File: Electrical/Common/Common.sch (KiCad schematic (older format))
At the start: 68 parts, among them J201 01x02, J202 01x04, J203 01x03, J204 01x04, J205 01x03, J206 USB_OTG, J207 01x04, J208 01x02, J209 01x04, J210 01x02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

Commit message: Completed Dual Stepper Layout. TODO: Via stitching.
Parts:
- removed J215: JST_3, Connectors_JST:JST_XH_B03B-XH-A_03x2.50mm_Straight, symbol Conn_01x03
- added J217: 2PostTerm, footprints:TerminalBlock_Custom_1x02.54mm, symbol Screw_Terminal_01x02
- added J218, J219: 01x02, Pin_Headers:Pin_Header_Straight_1x02_Pitch2.54mm, symbol Conn_01x02
- added R205, R206: 12K, Resistors_SMD:R_0603_HandSoldering, symbol R
- added RN208, RN209, RN210, RN211: 1K2, footprints:R_Array_1206x04, symbol R_Pack04
- J206: footprint Connectors_USB:USB_Micro-B_Molex-105017-0001 -> footprints:USB_Micro-B_Molex-105017-0001_CircularHoles
- renumbered J216 to J215, J217 to J216
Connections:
- net labels added: GPIO_52, gpio1_12, usb1_5V
- net labels removed: +BATT, GPIO_44, batt_temp, gpio1_20
- wire segments 263 -> 286
- no-connect marks 2 -> 4
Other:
- moved on the sheet: J213, J214, J215, J216

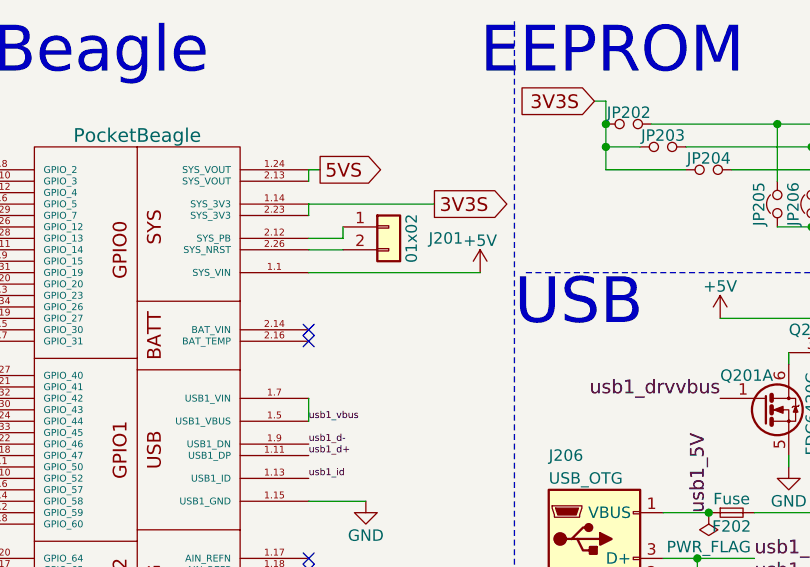
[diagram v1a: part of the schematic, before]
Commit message: Added a diode to the stepper fault/3v3 supply to ensure fault remains low when RESET/PMIC_OUT_PGOOD is low.
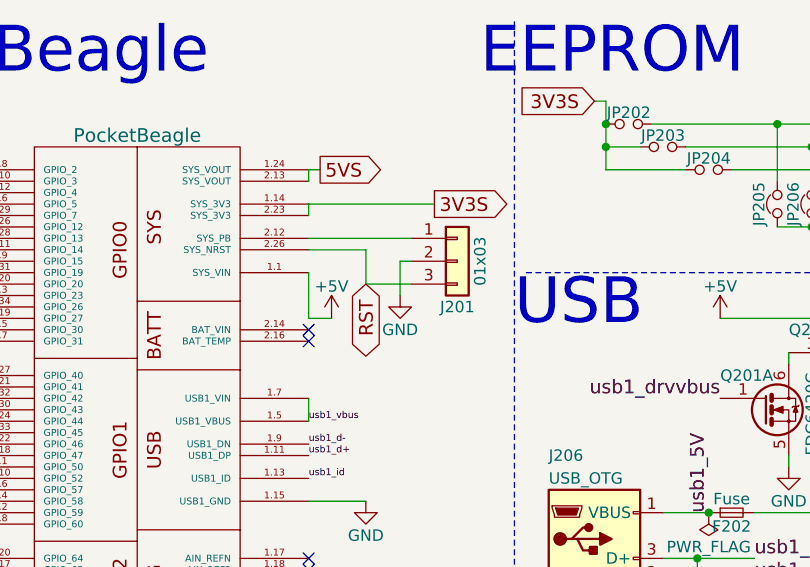
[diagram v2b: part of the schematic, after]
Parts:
- removed J201: 01x02, Pin_Headers:Pin_Header_Straight_1x02_Pitch2.54mm, symbol Conn_01x02
- added J201: 01x03, Pin_Headers:Pin_Header_Straight_1x03_Pitch2.54mm, symbol Conn_01x03
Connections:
- net labels added: RST
- wire segments 286 -> 290

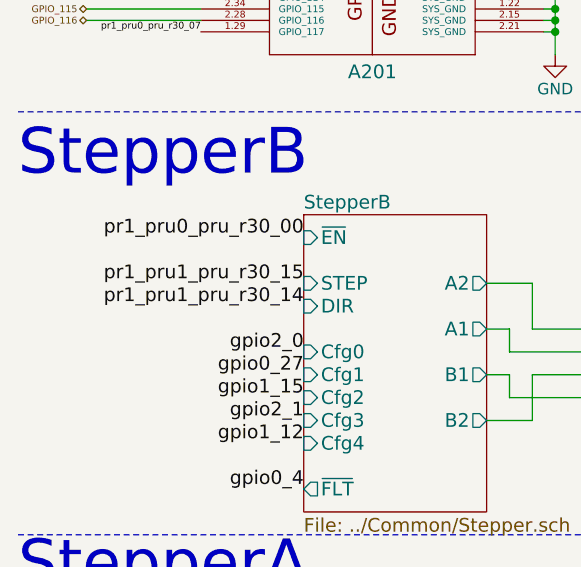
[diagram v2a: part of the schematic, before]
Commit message: Switched two pins for easier routing on quad board.
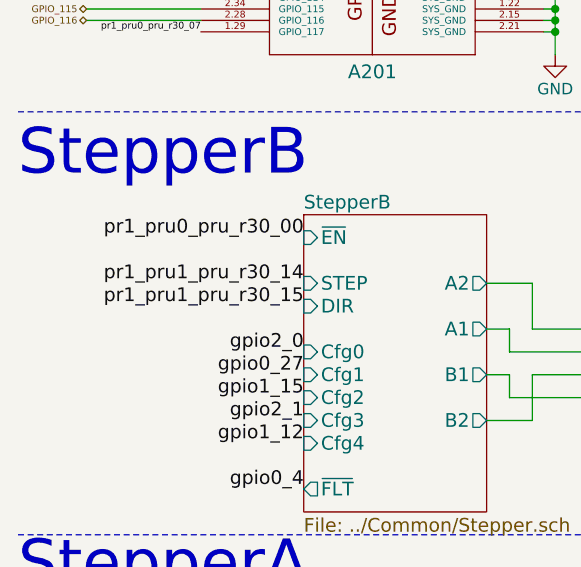
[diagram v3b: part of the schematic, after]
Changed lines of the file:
@@
 LIBS:allegro
 LIBS:mechanical
-LIBS:Dual-cache
+LIBS:Quad-cache
 EELAYER 25 0
 EELAYER END
 $Descr A4 11693 8268
 encoding utf-8
-Sheet 2 4
+Sheet 2 6
 Title ""
 Date ""
@@
 Adjustable Power Supply
 $Comp
-L GND #PWR211
+L GND #PWR04
 U 1 1 5A4ECB5E
 P 2850 3750
-F 0 "#PWR211" H 2850 3500 50  0001 C CNN
+F 0 "#PWR04" H 2850 3500 50  0001 C CNN
 F 1 "GND" H 2850 3600 50  0000 C CNN
 F 2 "" H 2850 3750 50  0001 C CNN
@@
 $EndComp
 $Comp
-L GND #PWR205
+L GND #PWR05
 U 1 1 5A5034AE
 P 8950 1900
-F 0 "#PWR205" H 8950 1650 50  0001 C CNN
+F 0 "#PWR05" H 8950 1650 50  0001 C CNN
 F 1 "GND" H 8950 1750 50  0000 C CNN
 F 2 "" H 8950 1900 50  0001 C CNN
@@
 $EndComp
 $Comp
-L GND #PWR210
+L GND #PWR06
 U 1 1 5A50411A
 P 8950 3550
-F 0 "#PWR210" H 8950 3300 50  0001 C CNN
+F 0 "#PWR06" H 8950 3300 50  0001 C CNN
 F 1 "GND" H 8950 3400 50  0000 C CNN
 F 2 "" H 8950 3550 50  0001 C CNN
@@
 $EndComp
 $Comp
-L PWR_FLAG #FLG202
+L PWR_FLAG #FLG07
 U 1 1 5A50A965
 P 7800 4350
-F 0 "#FLG202" H 7800 4425 50  0001 C CNN
+F 0 "#FLG07" H 7800 4425 50  0001 C CNN
 F 1 "PWR_FLAG" H 7800 4500 50  0000 C CNN
 F 2 "" H 7800 4350 50  0001 C CNN
@@
 Vin
 $Comp
-L GND #PWR219
+L GND #PWR08
 U 1 1 5A50A9F8
 P 7800 4900
-F 0 "#PWR219" H 7800 4650 50  0001 C CNN
+F 0 "#PWR08" H 7800 4650 50  0001 C CNN
 F 1 "GND" H 7800 4750 50  0000 C CNN
 F 2 "" H 7800 4900 50  0001 C CNN
@@
 Vadj
 $Comp
-L +5V #PWR212
+L +5V #PWR09
 U 1 1 5A50AB43
 P 8400 4250
-F 0 "#PWR212" H 8400 4100 50  0001 C CNN
+F 0 "#PWR09" H 8400 4100 50  0001 C CNN
 F 1 "+5V" H 8400 4390 50  0000 C CNN
 F 2 "" H 8400 4250 50  0001 C CNN
@@
 $EndComp
 $Comp
-L GND #PWR216
+L GND #PWR010
 U 1 1 5A50ABA3
 P 9150 4450
-F 0 "#PWR216" H 9150 4200 50  0001 C CNN
+F 0 "#PWR010" H 9150 4200 50  0001 C CNN
 F 1 "GND" H 9150 4300 50  0000 C CNN
 F 2 "" H 9150 4450 50  0001 C CNN
@@
 $EndComp
 $Comp
-L GND #PWR215
+L GND #PWR011
 U 1 1 5A50ABE1
 P 8400 4450
-F 0 "#PWR215" H 8400 4200 50  0001 C CNN
+F 0 "#PWR011" H 8400 4200 50  0001 C CNN
 F 1 "GND" H 8400 4300 50  0000 C CNN
 F 2 "" H 8400 4450 50  0001 C CNN
@@
 $EndComp
 $Comp
-L +5V #PWR223
+L +5V #PWR012
 U 1 1 5A50ACF1
 P 7250 5200
-F 0 "#PWR223" H 7250 5050 50  0001 C CNN
+F 0 "#PWR012" H 7250 5050 50  0001 C CNN
 F 1 "+5V" H 7250 5340 50  0000 C CNN
 F 2 "" H 7250 5200 50  0001 C CNN
@@
 $EndSheet
 $Comp
-L +5V #PWR203
+L +5V #PWR013
 U 1 1 5A55A7CC
 P 2900 1800
-F 0 "#PWR203" H 2900 1650 50  0001 C CNN
+F 0 "#PWR013" H 2900 1650 50  0001 C CNN
 F 1 "+5V" H 2900 1940 50  0000 C CNN
 F 2 "" H 2900 1800 50  0001 C CNN
@@
 Text Label 1750 4550 2    60   ~ 0
 pr1_pru0_pru_r30_00
+Text Label 1750 4850 2    60   ~ 0
+pr1_pru1_pru_r30_15
 Text Label 1750 4750 2    60   ~ 0
-pr1_pru1_pru_r30_15
-Text Label 1750 4850 2    60   ~ 0
 pr1_pru1_pru_r30_14
 Text Label 1750 5050 2    60   ~ 0
@@
 $EndComp
 $Comp
-L GND #PWR218
+L GND #PWR014
 U 1 1 5A57243C
 P 4950 4900
-F 0 "#PWR218" H 4950 4650 50  0001 C CNN
+F 0 "#PWR014" H 4950 4650 50  0001 C CNN
 F 1 "GND" H 4950 4750 50  0000 C CNN
 F 2 "" H 4950 4900 50  0001 C CNN
@@
 $EndComp
 $Comp
-L GND #PWR227
+L GND #PWR015
 U 1 1 5A57262A
 P 5400 5850
-F 0 "#PWR227" H 5400 5600 50  0001 C CNN
+F 0 "#PWR015" H 5400 5600 50  0001 C CNN
 F 1 "GND" H 5400 5700 50  0000 C CNN
 F 2 "" H 5400 5850 50  0001 C CNN
@@
 $EndComp
 $Comp
-L GND #PWR213
+L GND #PWR016
 U 1 1 5A576111
 P 6300 4400
-F 0 "#PWR213" H 6300 4150 50  0001 C CNN
+F 0 "#PWR016" H 6300 4150 50  0001 C CNN
 F 1 "GND" H 6300 4250 50  0000 C CNN
 F 2 "" H 6300 4400 50  0001 C CNN
@@
 AIN_5V_3
 $Comp
-L GND #PWR231
+L GND #PWR017
 U 1 1 5A57FE72
 P 4800 7600
-F 0 "#PWR231" H 4800 7350 50  0001 C CNN
+F 0 "#PWR017" H 4800 7350 50  0001 C CNN
 F 1 "GND" H 4800 7450 50  0000 C CNN
 F 2 "" H 4800 7600 50  0001 C CNN
@@
 $EndComp
 $Comp
-L GND #PWR222
+L GND #PWR018
 U 1 1 5A589958
 P 4350 5200
-F 0 "#PWR222" H 4350 4950 50  0001 C CNN
+F 0 "#PWR018" H 4350 4950 50  0001 C CNN
 F 1 "GND" H 4350 5050 50  0000 C CNN
 F 2 "" H 4350 5200 50  0001 C CNN
@@
 3V3S
 $Comp
-L GND #PWR201
+L GND #PWR019
 U 1 1 5A56CE51
 P 5800 1400
-F 0 "#PWR201" H 5800 1150 50  0001 C CNN
+F 0 "#PWR019" H 5800 1150 50  0001 C CNN
 F 1 "GND" H 5800 1250 50  0000 C CNN
 F 2 "" H 5800 1400 50  0001 C CNN
@@
 $EndComp
 $Comp
-L GND #PWR208
+L GND #PWR020
 U 1 1 5A581D55
 P 4200 3450
-F 0 "#PWR208" H 4200 3200 50  0001 C CNN
+F 0 "#PWR020" H 4200 3200 50  0001 C CNN
 F 1 "GND" H 4200 3300 50  0000 C CNN
 F 2 "" H 4200 3450 50  0001 C CNN
@@
 $EndComp
 $Comp
-L GND #PWR207
+L GND #PWR021
 U 1 1 5A582263
 P 3050 2600
-F 0 "#PWR207" H 3050 2350 50  0001 C CNN
+F 0 "#PWR021" H 3050 2350 50  0001 C CNN
 F 1 "GND" H 3050 2450 50  0000 C CNN
 F 2 "" H 3050 2600 50  0001 C CNN
@@
 usb1_d-
 $Comp
-L +5V #PWR204
+L +5V #PWR022
 U 1 1 5A583964
 P 4600 1800
-F 0 "#PWR204" H 4600 1650 50  0001 C CNN
+F 0 "#PWR022" H 4600 1650 50  0001 C CNN
 F 1 "+5V" H 4600 1940 50  0000 C CNN
 F 2 "" H 4600 1800 50  0001 C CNN
@@
 $EndComp
 $Comp
-L GND #PWR206
+L GND #PWR023
 U 1 1 5A586591
 P 4900 2450
-F 0 "#PWR206" H 4900 2200 50  0001 C CNN
+F 0 "#PWR023" H 4900 2200 50  0001 C CNN
 F 1 "GND" H 4900 2300 50  0000 C CNN
 F 2 "" H 4900 2450 50  0001 C CNN
@@
 	4500 3350 4400 3350
 $Comp
-L GND #PWR209
+L GND #PWR024
 U 1 1 5A5906F7
 P 5300 3450
-F 0 "#PWR209" H 5300 3200 50  0001 C CNN
+F 0 "#PWR024" H 5300 3200 50  0001 C CNN
 F 1 "GND" H 5300 3300 50  0000 C CNN
 F 2 "" H 5300 3450 50  0001 C CNN
@@
 $EndComp
 $Comp
-L GND #PWR214
+L GND #PWR025
 U 1 1 5A59F19E
 P 3200 4450
-F 0 "#PWR214" H 3200 4200 50  0001 C CNN
+F 0 "#PWR025" H 3200 4200 50  0001 C CNN
 F 1 "GND" H 3200 4300 50  0000 C CNN
 F 2 "" H 3200 4450 50  0001 C CNN
@@
 $EndComp
 $Comp
-L GND #PWR230
+L GND #PWR026
 U 1 1 5A59F7FF
 P 3700 6350
-F 0 "#PWR230" H 3700 6100 50  0001 C CNN
+F 0 "#PWR026" H 3700 6100 50  0001 C CNN
 F 1 "GND" H 3700 6200 50  0000 C CNN
 F 2 "" H 3700 6350 50  0001 C CNN
@@
 Connection ~ 7800 4800
 $Comp
-L PWR_FLAG #FLG203
+L PWR_FLAG #FLG027
 U 1 1 5A590642
 P 7950 4800
-F 0 "#FLG203" H 7950 4875 50  0001 C CNN
+F 0 "#FLG027" H 7950 4875 50  0001 C CNN
 F 1 "PWR_FLAG" H 7950 4950 50  0000 C CNN
 F 2 "" H 7950 4800 50  0001 C CNN
@@
 	7950 4800 7800 4800
 $Comp
-L PWR_FLAG #FLG204
+L PWR_FLAG #FLG028
 U 1 1 5A590F89
 P 7000 5100
-F 0 "#FLG204" H 7000 5175 50  0001 C CNN
+F 0 "#FLG028" H 7000 5175 50  0001 C CNN
 F 1 "PWR_FLAG" H 7000 5250 50  0000 C CNN
 F 2 "" H 7000 5100 50  0001 C CNN
@@
 Connection ~ 6700 5100
 $Comp
-L PWR_FLAG #FLG205
+L PWR_FLAG #FLG029
 U 1 1 5A5913B1
 P 6950 5200
-F 0 "#FLG205" H 6950 5275 50  0001 C CNN
+F 0 "#FLG029" H 6950 5275 50  0001 C CNN
 F 1 "PWR_FLAG" H 6950 5350 50  0000 C CNN
 F 2 "" H 6950 5200 50  0001 C CNN
@@
 Connection ~ 6950 5200
 $Comp
-L PWR_FLAG #FLG201
+L PWR_FLAG #FLG030
 U 1 1 5A592059
 P 4550 2650
-F 0 "#FLG201" H 4550 2725 50  0001 C CNN
+F 0 "#FLG030" H 4550 2725 50  0001 C CNN
 F 1 "PWR_FLAG" H 4550 2800 50  0000 C CNN
 F 2 "" H 4550 2650 50  0001 C CNN
@@
 $EndComp
 $Comp
-L GND #PWR229
+L GND #PWR031
 U 1 1 5A5A5D04
 P 8850 6300
-F 0 "#PWR229" H 8850 6050 50  0001 C CNN
+F 0 "#PWR031" H 8850 6050 50  0001 C CNN
 F 1 "GND" H 8850 6150 50  0000 C CNN
 F 2 "" H 8850 6300 50  0001 C CNN
@@
 $EndComp
 $Comp
-L GND #PWR220
+L GND #PWR032
 U 1 1 5A5BF7A7
 P 9150 5000
-F 0 "#PWR220" H 9150 4750 50  0001 C CNN
+F 0 "#PWR032" H 9150 4750 50  0001 C CNN
 F 1 "GND" H 9150 4850 50  0000 C CNN
 F 2 "" H 9150 5000 50  0001 C CNN
@@
 $EndComp
 $Comp
-L GND #PWR217
+L GND #PWR033
 U 1 1 5A5C0770
 P 10150 4450
-F 0 "#PWR217" H 10150 4200 50  0001 C CNN
+F 0 "#PWR033" H 10150 4200 50  0001 C CNN
 F 1 "GND" H 10150 4300 50  0000 C CNN
 F 2 "" H 10150 4450 50  0001 C CNN
@@
 $EndComp
 $Comp
-L GND #PWR221
+L GND #PWR034
 U 1 1 5A5E1379
 P 10150 5000
-F 0 "#PWR221" H 10150 4750 50  0001 C CNN
+F 0 "#PWR034" H 10150 4750 50  0001 C CNN
 F 1 "GND" H 10150 4850 50  0000 C CNN
 F 2 "" H 10150 5000 50  0001 C CNN
@@
 	9250 5500 9250 5700
 $Comp
-L GND #PWR224
+L GND #PWR035
 U 1 1 5A5EB0DE
 P 9250 5700
-F 0 "#PWR224" H 9250 5450 50  0001 C CNN
+F 0 "#PWR035" H 9250 5450 50  0001 C CNN
 F 1 "GND" H 9250 5550 50  0000 C CNN
 F 2 "" H 9250 5700 50  0001 C CNN
@@
 	10750 5500 10750 5700
 $Comp
-L GND #PWR226
+L GND #PWR036
 U 1 1 5A5EBF7E
 P 10750 5700
-F 0 "#PWR226" H 10750 5450 50  0001 C CNN
+F 0 "#PWR036" H 10750 5450 50  0001 C CNN
 F 1 "GND" H 10750 5550 50  0000 C CNN
 F 2 "" H 10750 5700 50  0001 C CNN
@@
 	10150 5500 10150 6300
 $Comp
-L GND #PWR225
+L GND #PWR037
 U 1 1 5A5EF63A
 P 9750 5700
-F 0 "#PWR225" H 9750 5450 50  0001 C CNN
+F 0 "#PWR037" H 9750 5450 50  0001 C CNN
 F 1 "GND" H 9750 5550 50  0000 C CNN
 F 2 "" H 9750 5700 50  0001 C CNN
@@
 	10750 5950 10650 5950
 $Comp
-L GND #PWR228
+L GND #PWR038
 U 1 1 5A5F1ED1
 P 10650 6150
-F 0 "#PWR228" H 10650 5900 50  0001 C CNN
+F 0 "#PWR038" H 10650 5900 50  0001 C CNN
 F 1 "GND" H 10650 6000 50  0000 C CNN
 F 2 "" H 10650 6150 50  0001 C CNN
@@
 	3050 1650 3250 1650
 $Comp
-L GND #PWR202
+L GND #PWR039
 U 1 1 5A62C26E
 P 3200 1700
-F 0 "#PWR202" H 3200 1450 50  0001 C CNN
+F 0 "#PWR039" H 3200 1450 50  0001 C CNN
 F 1 "GND" H 3200 1550 50  0000 C CNN
 F 2 "" H 3200 1700 50  0001 C CNN

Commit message: fixed unconnected pad 6 on RN201
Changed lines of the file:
@@
 LIBS:allegro
 LIBS:mechanical
-LIBS:Quad-cache
+LIBS:Dual-cache
 EELAYER 25 0
 EELAYER END
 $Descr A4 11693 8268
 encoding utf-8
-Sheet 2 6
+Sheet 2 4
 Title ""
 Date ""
@@
 Adjustable Power Supply
 $Comp
-L GND #PWR04
+L GND #PWR06
 U 1 1 5A4ECB5E
 P 2850 3750
-F 0 "#PWR04" H 2850 3500 50  0001 C CNN
+F 0 "#PWR06" H 2850 3500 50  0001 C CNN
 F 1 "GND" H 2850 3600 50  0000 C CNN
 F 2 "" H 2850 3750 50  0001 C CNN
@@
 $EndComp
 $Comp
-L GND #PWR05
+L GND #PWR07
 U 1 1 5A5034AE
 P 8950 1900
-F 0 "#PWR05" H 8950 1650 50  0001 C CNN
+F 0 "#PWR07" H 8950 1650 50  0001 C CNN
 F 1 "GND" H 8950 1750 50  0000 C CNN
 F 2 "" H 8950 1900 50  0001 C CNN
@@
 $EndComp
 $Comp
-L GND #PWR06
+L GND #PWR08
 U 1 1 5A50411A
 P 8950 3550
-F 0 "#PWR06" H 8950 3300 50  0001 C CNN
+F 0 "#PWR08" H 8950 3300 50  0001 C CNN
 F 1 "GND" H 8950 3400 50  0000 C CNN
 F 2 "" H 8950 3550 50  0001 C CNN
@@
 $EndComp
 $Comp
-L PWR_FLAG #FLG07
+L PWR_FLAG #FLG09
 U 1 1 5A50A965
 P 7800 4350
-F 0 "#FLG07" H 7800 4425 50  0001 C CNN
+F 0 "#FLG09" H 7800 4425 50  0001 C CNN
 F 1 "PWR_FLAG" H 7800 4500 50  0000 C CNN
 F 2 "" H 7800 4350 50  0001 C CNN
@@
 Vin
 $Comp
-L GND #PWR08
+L GND #PWR010
 U 1 1 5A50A9F8
 P 7800 4900
-F 0 "#PWR08" H 7800 4650 50  0001 C CNN
+F 0 "#PWR010" H 7800 4650 50  0001 C CNN
 F 1 "GND" H 7800 4750 50  0000 C CNN
 F 2 "" H 7800 4900 50  0001 C CNN
@@
 Vadj
 $Comp
-L +5V #PWR09
+L +5V #PWR011
 U 1 1 5A50AB43
 P 8400 4250
-F 0 "#PWR09" H 8400 4100 50  0001 C CNN
+F 0 "#PWR011" H 8400 4100 50  0001 C CNN
 F 1 "+5V" H 8400 4390 50  0000 C CNN
 F 2 "" H 8400 4250 50  0001 C CNN
@@
 $EndComp
 $Comp
-L GND #PWR010
+L GND #PWR012
 U 1 1 5A50ABA3
 P 9150 4450
-F 0 "#PWR010" H 9150 4200 50  0001 C CNN
+F 0 "#PWR012" H 9150 4200 50  0001 C CNN
 F 1 "GND" H 9150 4300 50  0000 C CNN
 F 2 "" H 9150 4450 50  0001 C CNN
@@
 $EndComp
 $Comp
-L GND #PWR011
+L GND #PWR013
 U 1 1 5A50ABE1
 P 8400 4450
-F 0 "#PWR011" H 8400 4200 50  0001 C CNN
+F 0 "#PWR013" H 8400 4200 50  0001 C CNN
 F 1 "GND" H 8400 4300 50  0000 C CNN
 F 2 "" H 8400 4450 50  0001 C CNN
@@
 $EndComp
 $Comp
-L +5V #PWR012
+L +5V #PWR014
 U 1 1 5A50ACF1
 P 7250 5200
-F 0 "#PWR012" H 7250 5050 50  0001 C CNN
+F 0 "#PWR014" H 7250 5050 50  0001 C CNN
 F 1 "+5V" H 7250 5340 50  0000 C CNN
 F 2 "" H 7250 5200 50  0001 C CNN
@@
 $EndSheet
 $Comp
-L +5V #PWR013
+L +5V #PWR015
 U 1 1 5A55A7CC
 P 2900 1800
-F 0 "#PWR013" H 2900 1650 50  0001 C CNN
+F 0 "#PWR015" H 2900 1650 50  0001 C CNN
 F 1 "+5V" H 2900 1940 50  0000 C CNN
 F 2 "" H 2900 1800 50  0001 C CNN
@@
 $EndComp
 $Comp
-L GND #PWR014
+L GND #PWR016
 U 1 1 5A57243C
 P 4950 4900
-F 0 "#PWR014" H 4950 4650 50  0001 C CNN
+F 0 "#PWR016" H 4950 4650 50  0001 C CNN
 F 1 "GND" H 4950 4750 50  0000 C CNN
 F 2 "" H 4950 4900 50  0001 C CNN
@@
 $EndComp
 $Comp
-L GND #PWR015
+L GND #PWR017
 U 1 1 5A57262A
 P 5400 5850
-F 0 "#PWR015" H 5400 5600 50  0001 C CNN
+F 0 "#PWR017" H 5400 5600 50  0001 C CNN
 F 1 "GND" H 5400 5700 50  0000 C CNN
 F 2 "" H 5400 5850 50  0001 C CNN
@@
 $EndComp
 $Comp
-L GND #PWR016
+L GND #PWR018
 U 1 1 5A576111
 P 6300 4400
-F 0 "#PWR016" H 6300 4150 50  0001 C CNN
+F 0 "#PWR018" H 6300 4150 50  0001 C CNN
 F 1 "GND" H 6300 4250 50  0000 C CNN
 F 2 "" H 6300 4400 50  0001 C CNN
@@
 AIN_5V_3
 $Comp
-L GND #PWR017
+L GND #PWR019
 U 1 1 5A57FE72
 P 4800 7600
-F 0 "#PWR017" H 4800 7350 50  0001 C CNN
+F 0 "#PWR019" H 4800 7350 50  0001 C CNN
 F 1 "GND" H 4800 7450 50  0000 C CNN
 F 2 "" H 4800 7600 50  0001 C CNN
@@
 $EndComp
 $Comp
-L GND #PWR018
+L GND #PWR020
 U 1 1 5A589958
 P 4350 5200
-F 0 "#PWR018" H 4350 4950 50  0001 C CNN
+F 0 "#PWR020" H 4350 4950 50  0001 C CNN
 F 1 "GND" H 4350 5050 50  0000 C CNN
 F 2 "" H 4350 5200 50  0001 C CNN
@@
 3V3S
 $Comp
-L GND #PWR019
+L GND #PWR021
 U 1 1 5A56CE51
 P 5800 1400
-F 0 "#PWR019" H 5800 1150 50  0001 C CNN
+F 0 "#PWR021" H 5800 1150 50  0001 C CNN
 F 1 "GND" H 5800 1250 50  0000 C CNN
 F 2 "" H 5800 1400 50  0001 C CNN
@@
 $EndComp
 $Comp
-L GND #PWR020
+L GND #PWR022
 U 1 1 5A581D55
 P 4200 3450
-F 0 "#PWR020" H 4200 3200 50  0001 C CNN
+F 0 "#PWR022" H 4200 3200 50  0001 C CNN
 F 1 "GND" H 4200 3300 50  0000 C CNN
 F 2 "" H 4200 3450 50  0001 C CNN
@@
 $EndComp
 $Comp
-L GND #PWR021
+L GND #PWR023
 U 1 1 5A582263
 P 3050 2600
-F 0 "#PWR021" H 3050 2350 50  0001 C CNN
+F 0 "#PWR023" H 3050 2350 50  0001 C CNN
 F 1 "GND" H 3050 2450 50  0000 C CNN
 F 2 "" H 3050 2600 50  0001 C CNN
@@
 usb1_d-
 $Comp
-L +5V #PWR022
+L +5V #PWR024
 U 1 1 5A583964
 P 4600 1800
-F 0 "#PWR022" H 4600 1650 50  0001 C CNN
+F 0 "#PWR024" H 4600 1650 50  0001 C CNN
 F 1 "+5V" H 4600 1940 50  0000 C CNN
 F 2 "" H 4600 1800 50  0001 C CNN
@@
 $EndComp
 $Comp
-L GND #PWR023
+L GND #PWR025
 U 1 1 5A586591
 P 4900 2450
-F 0 "#PWR023" H 4900 2200 50  0001 C CNN
+F 0 "#PWR025" H 4900 2200 50  0001 C CNN
 F 1 "GND" H 4900 2300 50  0000 C CNN
 F 2 "" H 4900 2450 50  0001 C CNN
@@
 	4450 5200 5000 5200
 Wire Wire Line
-	4350 5200 4350 5100
+	4350 5000 4350 5200
 Wire Wire Line
 	6200 950  7050 950
@@
 	4500 3350 4400 3350
 $Comp
-L GND #PWR024
+L GND #PWR026
 U 1 1 5A5906F7
 P 5300 3450
-F 0 "#PWR024" H 5300 3200 50  0001 C CNN
+F 0 "#PWR026" H 5300 3200 50  0001 C CNN
 F 1 "GND" H 5300 3300 50  0000 C CNN
 F 2 "" H 5300 3450 50  0001 C CNN
@@
 $EndComp
 $Comp
-L GND #PWR025
+L GND #PWR027
 U 1 1 5A59F19E
 P 3200 4450
-F 0 "#PWR025" H 3200 4200 50  0001 C CNN
+F 0 "#PWR027" H 3200 4200 50  0001 C CNN
 F 1 "GND" H 3200 4300 50  0000 C CNN
 F 2 "" H 3200 4450 50  0001 C CNN
@@
 $EndComp
 $Comp
-L GND #PWR026
+L GND #PWR028
 U 1 1 5A59F7FF
 P 3700 6350
-F 0 "#PWR026" H 3700 6100 50  0001 C CNN
+F 0 "#PWR028" H 3700 6100 50  0001 C CNN
 F 1 "GND" H 3700 6200 50  0000 C CNN
 F 2 "" H 3700 6350 50  0001 C CNN
@@
 Connection ~ 7800 4800
 $Comp
-L PWR_FLAG #FLG027
+L PWR_FLAG #FLG029
 U 1 1 5A590642
 P 7950 4800
-F 0 "#FLG027" H 7950 4875 50  0001 C CNN
+F 0 "#FLG029" H 7950 4875 50  0001 C CNN
 F 1 "PWR_FLAG" H 7950 4950 50  0000 C CNN
 F 2 "" H 7950 4800 50  0001 C CNN
@@
 	7950 4800 7800 4800
 $Comp
-L PWR_FLAG #FLG028
+L PWR_FLAG #FLG030
 U 1 1 5A590F89
 P 7000 5100
-F 0 "#FLG028" H 7000 5175 50  0001 C CNN
+F 0 "#FLG030" H 7000 5175 50  0001 C CNN
 F 1 "PWR_FLAG" H 7000 5250 50  0000 C CNN
 F 2 "" H 7000 5100 50  0001 C CNN
@@
 Connection ~ 6700 5100
 $Comp
-L PWR_FLAG #FLG029
+L PWR_FLAG #FLG031
 U 1 1 5A5913B1
 P 6950 5200
-F 0 "#FLG029" H 6950 5275 50  0001 C CNN
+F 0 "#FLG031" H 6950 5275 50  0001 C CNN
 F 1 "PWR_FLAG" H 6950 5350 50  0000 C CNN
 F 2 "" H 6950 5200 50  0001 C CNN
@@
 Connection ~ 6950 5200
 $Comp
-L PWR_FLAG #FLG030
+L PWR_FLAG #FLG032
 U 1 1 5A592059
 P 4550 2650
-F 0 "#FLG030" H 4550 2725 50  0001 C CNN
+F 0 "#FLG032" H 4550 2725 50  0001 C CNN
 F 1 "PWR_FLAG" H 4550 2800 50  0000 C CNN
 F 2 "" H 4550 2650 50  0001 C CNN
@@
 $EndComp
 $Comp
-L GND #PWR031
+L GND #PWR033
 U 1 1 5A5A5D04
 P 8850 6300
-F 0 "#PWR031" H 8850 6050 50  0001 C CNN
+F 0 "#PWR033" H 8850 6050 50  0001 C CNN
 F 1 "GND" H 8850 6150 50  0000 C CNN
 F 2 "" H 8850 6300 50  0001 C CNN
@@
 $EndComp
 $Comp
-L GND #PWR032
+L GND #PWR034
 U 1 1 5A5BF7A7
 P 9150 5000
-F 0 "#PWR032" H 9150 4750 50  0001 C CNN
+F 0 "#PWR034" H 9150 4750 50  0001 C CNN
 F 1 "GND" H 9150 4850 50  0000 C CNN
 F 2 "" H 9150 5000 50  0001 C CNN
@@
 $EndComp
 $Comp
-L GND #PWR033
+L GND #PWR035
 U 1 1 5A5C0770
 P 10150 4450
-F 0 "#PWR033" H 10150 4200 50  0001 C CNN
+F 0 "#PWR035" H 10150 4200 50  0001 C CNN
 F 1 "GND" H 10150 4300 50  0000 C CNN
 F 2 "" H 10150 4450 50  0001 C CNN
@@
 $EndComp
 $Comp
-L GND #PWR034
+L GND #PWR036
 U 1 1 5A5E1379
 P 10150 5000
-F 0 "#PWR034" H 10150 4750 50  0001 C CNN
+F 0 "#PWR036" H 10150 4750 50  0001 C CNN
 F 1 "GND" H 10150 4850 50  0000 C CNN
 F 2 "" H 10150 5000 50  0001 C CNN
@@
 	9250 5500 9250 5700
 $Comp
-L GND #PWR035
+L GND #PWR037
 U 1 1 5A5EB0DE
 P 9250 5700
-F 0 "#PWR035" H 9250 5450 50  0001 C CNN
+F 0 "#PWR037" H 9250 5450 50  0001 C CNN
 F 1 "GND" H 9250 5550 50  0000 C CNN
 F 2 "" H 9250 5700 50  0001 C CNN
@@
 	10750 5500 10750 5700
 $Comp
-L GND #PWR036
+L GND #PWR038
 U 1 1 5A5EBF7E
 P 10750 5700
-F 0 "#PWR036" H 10750 5450 50  0001 C CNN
+F 0 "#PWR038" H 10750 5450 50  0001 C CNN
 F 1 "GND" H 10750 5550 50  0000 C CNN
 F 2 "" H 10750 5700 50  0001 C CNN
@@
 	10150 5500 10150 6300
 $Comp
-L GND #PWR037
+L GND #PWR039
 U 1 1 5A5EF63A
 P 9750 5700
-F 0 "#PWR037" H 9750 5450 50  0001 C CNN
+F 0 "#PWR039" H 9750 5450 50  0001 C CNN
 F 1 "GND" H 9750 5550 50  0000 C CNN
 F 2 "" H 9750 5700 50  0001 C CNN
@@
 	10750 5950 10650 5950
 $Comp
-L GND #PWR038
+L GND #PWR040
 U 1 1 5A5F1ED1
 P 10650 6150
-F 0 "#PWR038" H 10650 5900 50  0001 C CNN
+F 0 "#PWR040" H 10650 5900 50  0001 C CNN
 F 1 "GND" H 10650 6000 50  0000 C CNN
 F 2 "" H 10650 6150 50  0001 C CNN
@@
 	3050 1650 3250 1650
 $Comp
-L GND #PWR039
+L GND #PWR041
 U 1 1 5A62C26E
 P 3200 1700
-F 0 "#PWR039" H 3200 1450 50  0001 C CNN
+F 0 "#PWR041" H 3200 1450 50  0001 C CNN
 F 1 "GND" H 3200 1550 50  0000 C CNN
 F 2 "" H 3200 1700 50  0001 C CNN
@@
 Text GLabel 3050 1650 3    60   BiDi ~ 0
 RST
+Connection ~ 4350 5100
 $EndSCHEMATC
